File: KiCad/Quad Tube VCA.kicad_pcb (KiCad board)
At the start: 2 copper layers, 162.6 x 100.3 mm, 224 parts, among them IC1 TL072, IC10 LM358, IC2 TL072, IC3 LM358, IC4 TL072, IC5 LM358, IC6 TL072, IC7 TL072, IC8 LM358, IC9 TL072

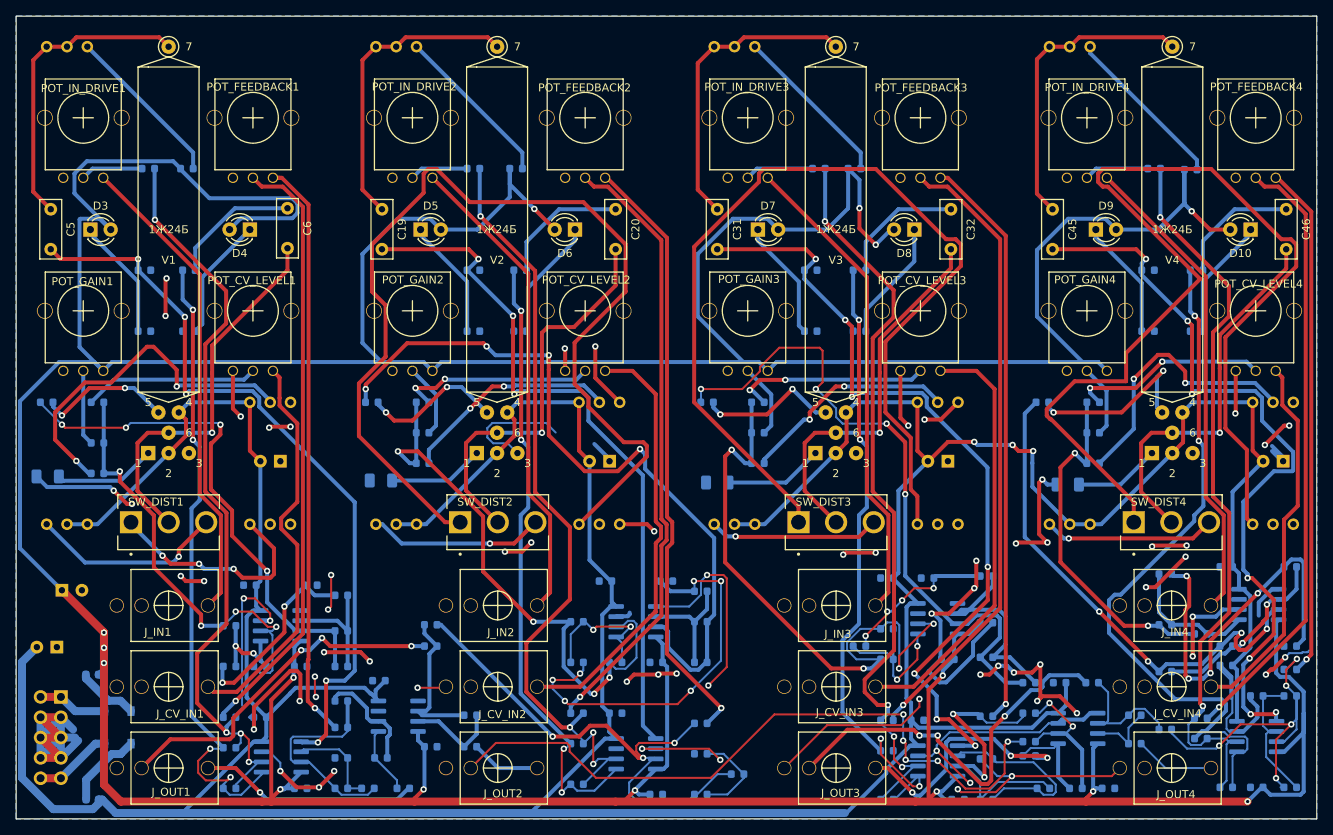
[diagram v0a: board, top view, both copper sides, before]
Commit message: adds inverting buffers, new layout
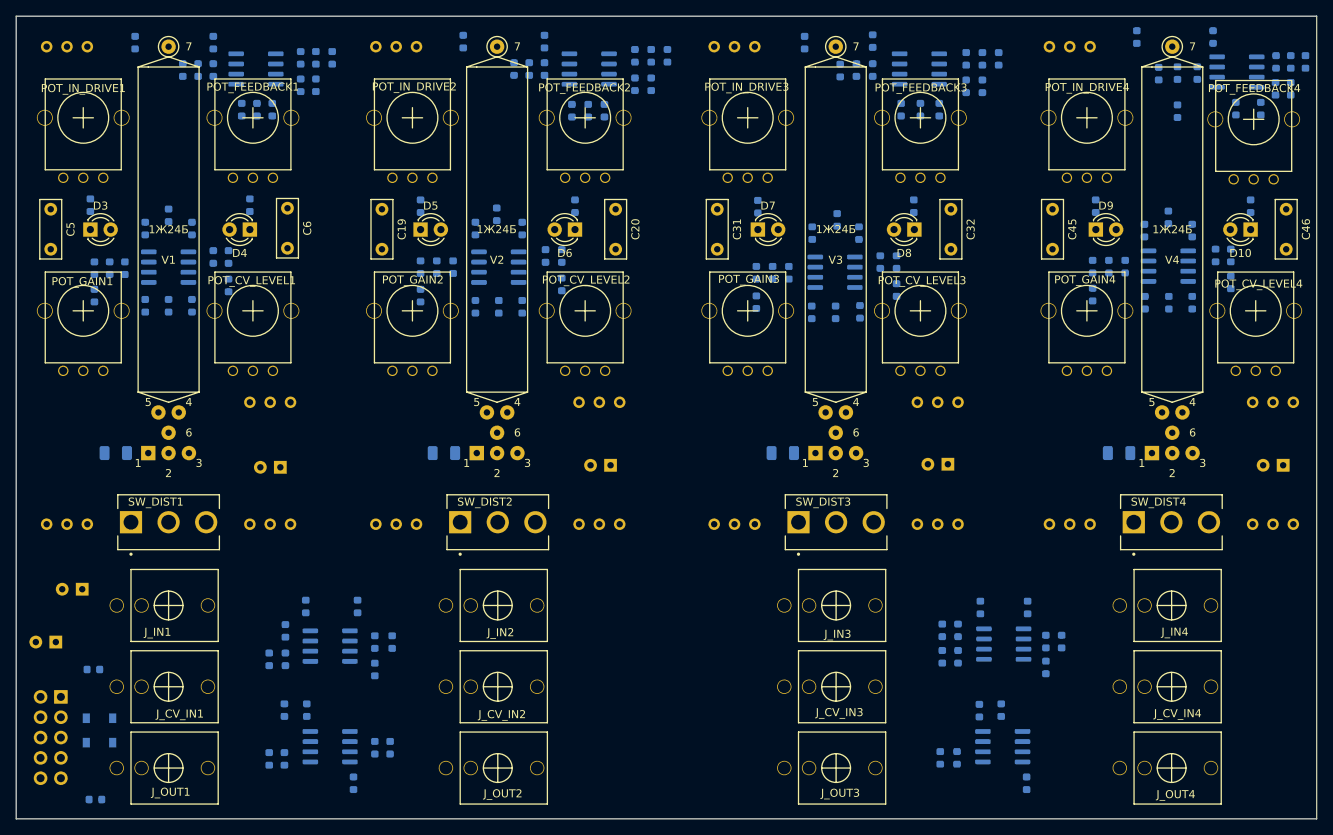
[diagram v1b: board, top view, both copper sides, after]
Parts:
- removed the IC4 at (143.5, 136.7)
- added C55: 100nf, Capacitor_SMD:C_0603_1608Metric, B.Cu at (108.2, 140.3)
- added C56: 100nf, Capacitor_SMD:C_0603_1608Metric, B.Cu at (102.4, 131.2)
- added C57: 100nf, Capacitor_SMD:C_0603_1608Metric, B.Cu at (192.3, 140.3)
- added C58: 100nf, Capacitor_SMD:C_0603_1608Metric, B.Cu at (186.4, 131.3)
- added IC11: TL072, Package_SO:SOIC-8_3.9x4.9mm_P1.27mm, B.Cu at (105.3, 135.8)
- added IC12: TL072, Package_SO:SOIC-8_3.9x4.9mm_P1.27mm, B.Cu at (189.4, 135.8)
- added IC9: TL072, Package_SO:SOIC-8_3.9x4.9mm_P1.27mm, B.Cu at (218.6, 51.4)
- added R100: 100k, Resistor_SMD:R_0603_1608Metric, B.Cu at (183.6, 137.2)
- added R101: 100k, Resistor_SMD:R_0603_1608Metric, B.Cu at (181.5, 137.2)
- added R96: 100k, Resistor_SMD:R_0603_1608Metric, B.Cu at (99.6, 137.3)
- added R97: 100k, Resistor_SMD:R_0603_1608Metric, B.Cu at (97.7, 137.3)
- added R98: 100k, Resistor_SMD:R_0603_1608Metric, B.Cu at (110.9, 135.9)
- added R99: 100k, Resistor_SMD:R_0603_1608Metric, B.Cu at (112.8, 135.9)
- moved IC4 96.8 mm to (137.7, 51.1), turned to 180 degrees
- moved C37 95.4 mm to (173.1, 47.6), turned to 90 degrees
- moved C22 95.1 mm to (132.1, 47.6), turned to 90 degrees
- moved C50 93.9 mm to (215.6, 47.1), turned to 90 degrees
- moved C11 93.9 mm to (90.7, 47.8), turned to 90 degrees
- moved IC6 93.5 mm to (178.9, 51.1), turned to 180 degrees
- moved R52 93.1 mm to (184.8, 49.8), turned to 90 degrees
- moved C30 92.8 mm to (171.1, 51.2), turned to 90 degrees
- moved R26 92.8 mm to (132.1, 51.1), turned to 90 degrees
- moved R50 92.3 mm to (173.1, 51.2), turned to 90 degrees
- moved C4 92.3 mm to (88.8, 51.2), turned to 90 degrees
- moved C18 91.9 mm to (130.2, 51.1), turned to 90 degrees
- moved R5 91.7 mm to (101.6, 49.7), turned to 90 degrees
- moved R28 91.3 mm to (143.4, 49.4), turned to 90 degrees
- moved R3 91.2 mm to (90.7, 51.2), turned to 90 degrees
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- renumbered IC6 to IC4, IC9 to IC6
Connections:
- IC4 pad 1: Net-(C29-Pad1) -> Net-(C17-Pad1)
- IC4 pad 2: Net-(C29-Pad2) -> Net-(C17-Pad2)
- IC4 pad 5: Net-(C31-Pad2) -> Net-(C19-Pad2)
- IC4 pad 6: Net-(C30-Pad1) -> Net-(C18-Pad1)
- IC4 pad 7: Net-(C30-Pad2) -> Net-(C18-Pad2)
- IC6 pad 1: Net-(C43-Pad1) -> Net-(C29-Pad1)
- IC6 pad 2: Net-(C43-Pad2) -> Net-(C29-Pad2)
- IC6 pad 5: Net-(C45-Pad2) -> Net-(C31-Pad2)
- IC6 pad 6: Net-(C44-Pad1) -> Net-(C30-Pad1)
- IC6 pad 7: Net-(C44-Pad2) -> Net-(C30-Pad2)
- R30 pad 2: Net-(J_OUT1-Pad2) -> Net-(IC11-Pad1)
- R54 pad 2: Net-(J_OUT2-Pad2) -> Net-(IC11-Pad7)
- R79 pad 2: Net-(J_OUT3-Pad2) -> Net-(IC12-Pad1)
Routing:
- net +12V: track 732.8 -> 0.00 mm, vias 15 -> 0
- net -12V: track 544.8 -> 0.00 mm, vias 3 -> 0
- net GND: track 426.5 -> 0.00 mm, vias 63 -> 0
- net Net-(SW_DIST4-Pad1): track 134.5 -> 0.00 mm
- net Net-(SW_DIST2-Pad1): track 130.4 -> 0.00 mm
- net Net-(SW_DIST3-Pad1): track 122.3 -> 0.00 mm
- net Net-(C31-Pad2): track 99.7 -> 0.00 mm, vias 7 -> 0
- net Net-(C17-Pad2): track 99.2 -> 0.00 mm, vias 4 -> 0
- net Net-(C24-Pad2): track 98.4 -> 0.00 mm, vias 4 -> 0
- net Net-(C3-Pad2): track 96.2 -> 0.00 mm, vias 4 -> 0
- net Net-(C29-Pad2): track 95.8 -> 0.00 mm, vias 4 -> 0
- net Net-(C45-Pad2): track 94.6 -> 0.00 mm, vias 7 -> 0
- net Net-(C5-Pad2): track 93.9 -> 0.00 mm, vias 5 -> 0
- net Net-(C43-Pad2): track 93.2 -> 0.00 mm, vias 2 -> 0
- net Net-(C43-Pad1): track 90.6 -> 0.00 mm, vias 2 -> 0
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- removed copper zone on B.Cu, net GND
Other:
- board text added: "Vālvs v1.2 PCB Design: Olly Berry"
- board text removed: "Vālvs v1.01 PCB Design: Olly Berry"

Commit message: routes new layout
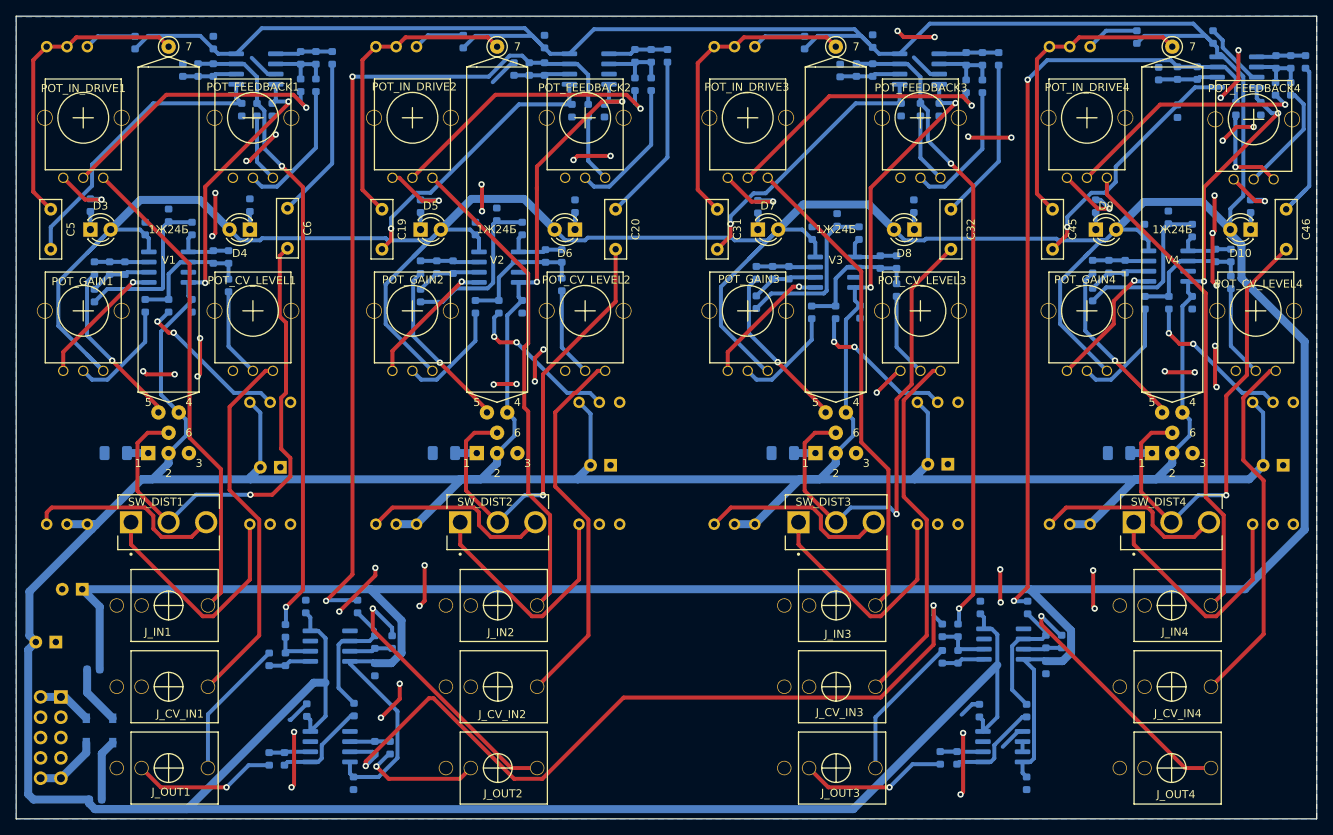
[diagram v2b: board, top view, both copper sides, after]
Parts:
- moved R30 8.70 mm to (108.3, 131.1)
- moved R79 3.18 mm to (192.3, 131.3)
- turned R24 to 270 degrees
- turned R48 to 270 degrees
- turned R72 to 270 degrees
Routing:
- net +12V: track 0.00 -> 770.8 mm
- net -12V: track 0.00 -> 723.4 mm, vias 0 -> 8
- net GND: track 0.00 -> 261.2 mm, vias 0 -> 55
- net Net-(C18-Pad2): track 0.00 -> 106.1 mm, vias 0 -> 2
- net Net-(IC11-Pad7): track 0.00 -> 98.8 mm, vias 0 -> 2
- net Net-(C44-Pad2): track 0.00 -> 98.6 mm, vias 0 -> 2
- net Net-(C30-Pad2): track 0.00 -> 80.6 mm, vias 0 -> 2
- net Net-(C4-Pad2): track 0.00 -> 79.8 mm, vias 0 -> 2
- net Net-(C6-Pad2): track 0.00 -> 63.5 mm, vias 0 -> 1
- net Net-(J_IN2-Pad3): track 0.00 -> 60.6 mm
- net Net-(C32-Pad2): track 0.00 -> 60.5 mm, vias 0 -> 1
- net Net-(J_IN3-Pad3): track 0.00 -> 60.4 mm
- net Net-(J_IN1-Pad3): track 0.00 -> 60.2 mm
- net Net-(J_IN4-Pad3): track 0.00 -> 60.2 mm
- net Net-(C46-Pad2): track 0.00 -> 58.0 mm, vias 0 -> 1
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- added copper zone on B.Cu, net GND

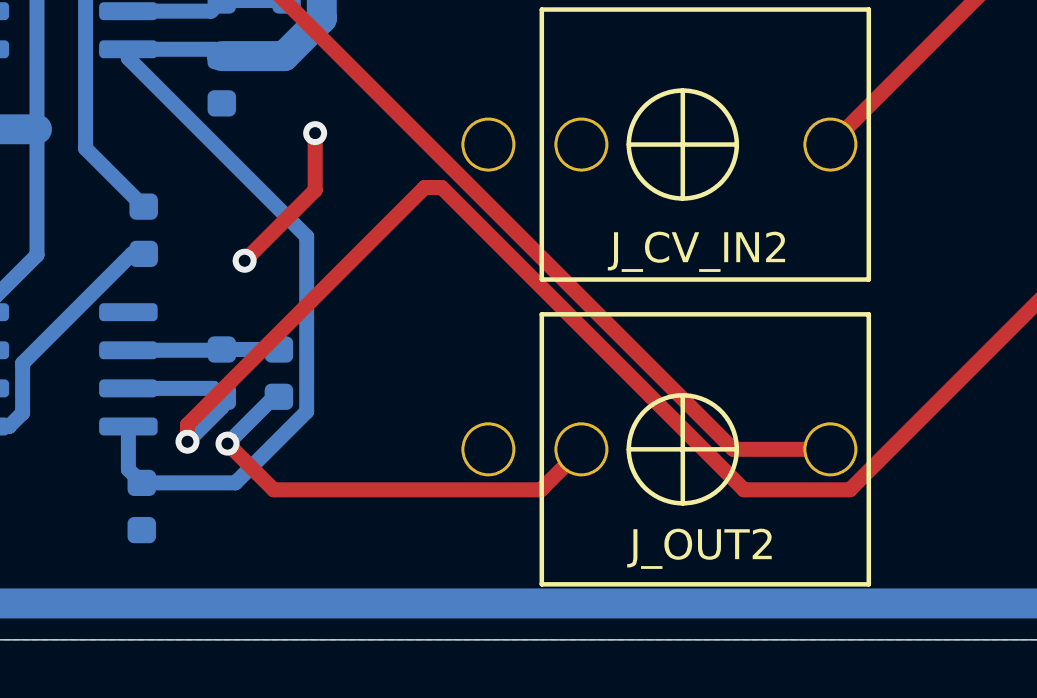
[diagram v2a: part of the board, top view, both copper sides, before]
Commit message: routes new layout
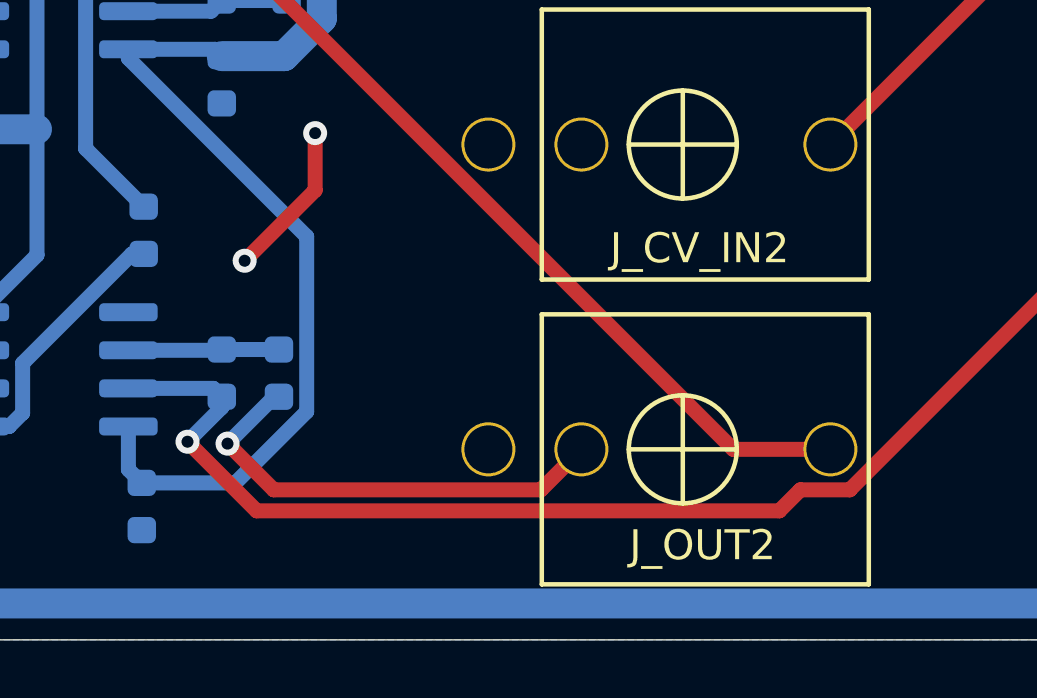
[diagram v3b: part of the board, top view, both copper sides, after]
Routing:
- net Net-(IC11-Pad7): track 98.8 -> 92.0 mm
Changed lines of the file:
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@@
     (thickness 1.6)
     (drawings 13)
-    (tracks 1191)
+    (tracks 1190)
     (zones 0)
     (modules 236)
@@
   (layers
     (0 F.Cu signal)
-    (31 B.Cu signal)
+    (31 B.Cu signal hide)
     (32 B.Adhes user)
     (33 F.Adhes user)
@@
     (35 F.Paste user)
     (36 B.SilkS user)
-    (37 F.SilkS user hide)
+    (37 F.SilkS user)
     (38 B.Mask user)
     (39 F.Mask user)
@@
     )
   )
-  (gr_text "[ H A R D W I R E D   E N G I N E E R I N G ]" (at 146.431 124.6505) (layer B.SilkS)
+  (gr_text "[ H A R D W I R E D   E N G I N E E R I N G ]" (at 146.3675 130.8735) (layer B.SilkS)
     (effects (font (size 0.5 0.7) (thickness 0.1)) (justify mirror))
   )
-  (gr_text "Vālvs v1.2\nPCB Design: Olly Berry" (at 146.431 129.6035) (layer B.SilkS)
+  (gr_text "Vālvs v1.2\nPCB Design: Olly Berry" (at 146.3675 135.8265) (layer B.SilkS)
     (effects (font (size 1 1) (thickness 0.15)) (justify mirror))
   )
@@
     (effects (font (size 1 1) (thickness 0.15)))
   )
-  (gr_text Vālvs (at 146.431 119.761) (layer B.SilkS)
+  (gr_text Vālvs (at 146.3675 125.984) (layer B.SilkS)
     (effects (font (size 6 6) (thickness 1)) (justify mirror))
   )
@@
   (segment (start 180.709001 123.008001) (end 180.709001 118.11) (width 0.5) (layer F.Cu) (net 136))
   (segment (start 141.966001 129.620001) (end 174.097001 129.620001) (width 0.5) (layer F.Cu) (net 136))
-  (segment (start 118.202018 129.701982) (end 128.280037 139.780001) (width 0.5) (layer F.Cu) (net 136))
-  (segment (start 117.636333 129.701982) (end 118.202018 129.701982) (width 0.5) (layer F.Cu) (net 136))
   (segment (start 131.806001 139.780001) (end 141.966001 129.620001) (width 0.5) (layer F.Cu) (net 136))
-  (segment (start 109.728 137.610315) (end 117.636333 129.701982) (width 0.5) (layer F.Cu) (net 136))
-  (segment (start 128.280037 139.780001) (end 131.806001 139.780001) (width 0.5) (layer F.Cu) (net 136))
-  (segment (start 109.728 138.176) (end 109.728 137.610315) (width 0.5) (layer F.Cu) (net 136))
   (segment (start 180.709001 119.342501) (end 181.8005 120.434) (width 0.5) (layer B.Cu) (net 136))
   (segment (start 180.709001 118.11) (end 180.709001 119.342501) (width 0.5) (layer B.Cu) (net 136))
+  (segment (start 131.806001 139.780001) (end 130.158499 139.780001) (width 0.5) (layer F.Cu) (net 136))
+  (segment (start 112.032011 140.480011) (end 109.728 138.176) (width 0.5) (layer F.Cu) (net 136))
+  (segment (start 129.458489 140.480011) (end 112.032011 140.480011) (width 0.5) (layer F.Cu) (net 136))
+  (segment (start 130.158499 139.780001) (end 129.458489 140.480011) (width 0.5) (layer F.Cu) (net 136))
   (segment (start 110.8455 135.128) (end 110.871 135.1025) (width 0.5) (layer B.Cu) (net 137))
   (segment (start 107.758 135.128) (end 110.8455 135.128) (width 0.5) (layer B.Cu) (net 137))

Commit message: 1.2 pcb update
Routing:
- net Net-(C46-Pad2): track 58.0 -> 60.6 mm
- net GND: track 261.2 -> 261.8 mm

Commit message: 1.3 pcb update
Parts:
- removed C55, C56, C57, C58: 100nf, Capacitor_SMD:C_0603_1608Metric
- removed IC11, IC12: TL072, Package_SO:SOIC-8_3.9x4.9mm_P1.27mm
- removed R100, R101: 100k, Resistor_SMD:R_0603_1608Metric
- R13, R37, R61, R85: footprint Resistor_SMD:R_1206_3216Metric -> Resistor_SMD:R_1210_3225Metric
- R2, R25, R49, R73: value 100k -> 33k
- moved R99 80.2 mm to (192.5, 127.6)
- moved R98 69.9 mm to (179.6, 122.9)
- moved R96 16.1 mm to (97.7, 121.3)
- moved R97 14.3 mm to (108.2, 127.6)
- moved R55 0.51 mm to (183.8, 125.0)
- moved R57 0.51 mm to (181.8, 125.0)
- moved R79 0.20 mm to (192.5, 131.2)
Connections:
- IC2 pad 3: GND -> Net-(IC2-Pad3)
- IC2 pad 5: GND -> Net-(IC2-Pad5)
- IC7 pad 3: GND -> Net-(IC7-Pad3)
- IC7 pad 5: GND -> Net-(IC7-Pad5)
- R30 pad 1: Net-(IC2-Pad6) -> Net-(IC2-Pad5)
- R30 pad 2: Net-(IC11-Pad1) -> Net-(J_OUT1-Pad2)
- R34 pad 1: Net-(IC2-Pad6) -> Net-(IC2-Pad5)
- R54 pad 1: Net-(IC7-Pad2) -> Net-(IC7-Pad3)
- R54 pad 2: Net-(IC11-Pad7) -> Net-(J_OUT2-Pad2)
- R58 pad 1: Net-(IC7-Pad2) -> Net-(IC7-Pad3)
- R79 pad 1: Net-(IC7-Pad6) -> Net-(IC7-Pad5)
- R79 pad 2: Net-(IC12-Pad1) -> Net-(J_OUT3-Pad2)
- R81 pad 1: Net-(IC7-Pad6) -> Net-(IC7-Pad5)
- R9 pad 1: Net-(IC2-Pad2) -> Net-(IC2-Pad3)
- R96 pad 1: Net-(IC11-Pad1) -> Net-(IC2-Pad2)
- R96 pad 2: Net-(IC11-Pad2) -> GND
- R97 pad 1: Net-(IC11-Pad2) -> Net-(IC2-Pad6)
- R97 pad 2: Net-(J_OUT1-Pad2) -> GND
- R98 pad 1: Net-(IC11-Pad7) -> Net-(IC7-Pad2)
- R98 pad 2: Net-(IC11-Pad6) -> GND
- R99 pad 1: Net-(IC11-Pad6) -> Net-(IC7-Pad6)
- R99 pad 2: Net-(J_OUT2-Pad2) -> GND
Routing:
- net Net-(IC11-Pad7): track 92.0 -> 0.00 mm, vias 2 -> 0
- net Net-(J_OUT2-Pad2): track 15.4 -> 66.4 mm, vias 1 -> 0
- net +12V: track 770.8 -> 731.0 mm
- net GND: track 261.8 -> 232.3 mm, vias 55 -> 49
- net -12V: track 723.4 -> 703.4 mm
- net Net-(IC2-Pad5): track 0.00 -> 14.1 mm
- net Net-(IC7-Pad5): track 0.00 -> 13.9 mm
- net Net-(J_OUT1-Pad2): track 18.1 -> 31.2 mm
- net Net-(J_OUT3-Pad2): track 18.6 -> 31.3 mm
- net Net-(IC11-Pad1): track 12.2 -> 0.00 mm
- net Net-(IC12-Pad1): track 12.1 -> 0.00 mm
- net Net-(IC7-Pad6): track 16.4 -> 9.80 mm
- net Net-(IC2-Pad6): track 16.9 -> 10.6 mm
- net Net-(IC12-Pad2): track 5.35 -> 0.00 mm
- net Net-(IC7-Pad3): track 0.00 -> 5.33 mm
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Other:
- board text added: "Vālvs v1.3 PCB Design: Olly Berry"
- board text removed: "Vālvs v1.2 PCB Design: Olly Berry"

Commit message: updates feedback resistor value for vca1
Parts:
- R7: value 100k -> 100R
